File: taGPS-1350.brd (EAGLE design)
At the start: 49.9 x 61.5 mm, 86 parts, among them IC1 MSP430FR698X(1)80-PIN_PN, IC3 FT232RL

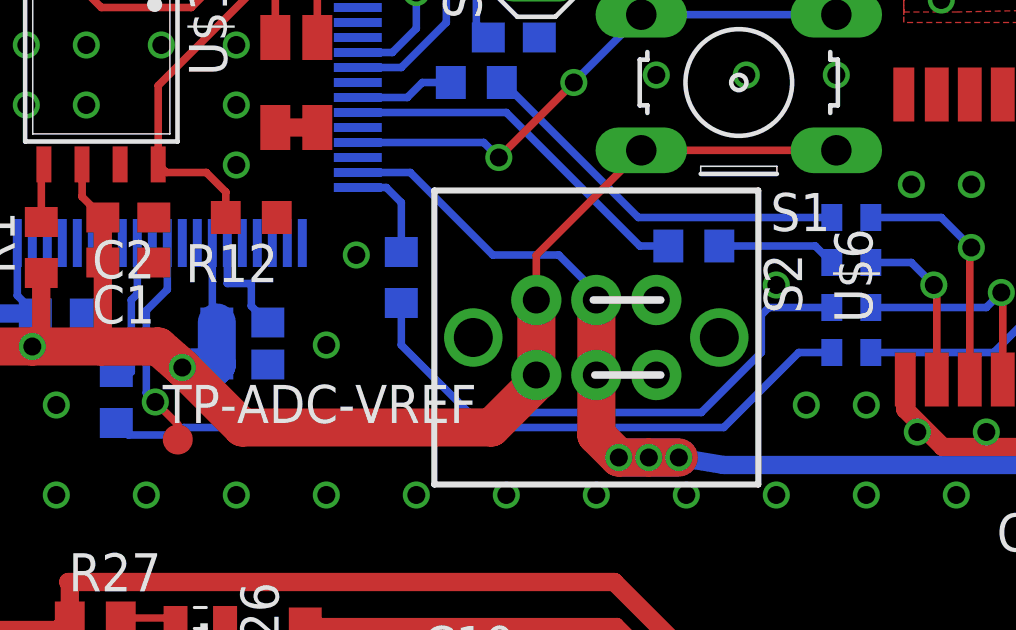
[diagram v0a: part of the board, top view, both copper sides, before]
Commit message: Fix 1350.brd timepulse resistor position
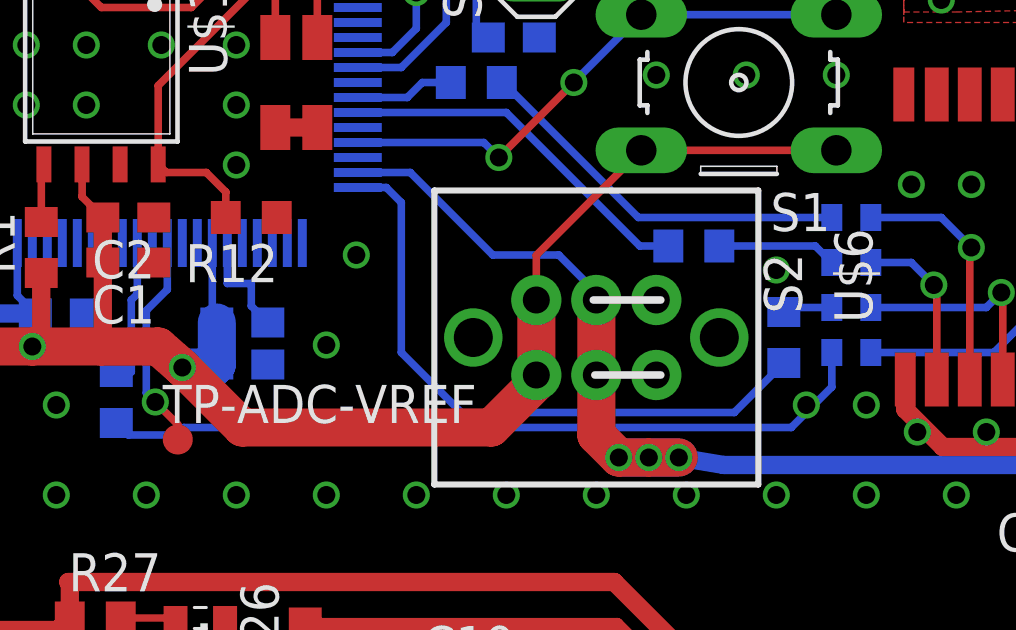
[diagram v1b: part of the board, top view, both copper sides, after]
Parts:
- moved R35 12.9 mm to (33.2, 33.2), turned to 90 degrees
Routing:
- net MB-GPS-TIMEPULSE: track 3.31 -> 20.9 mm
- net N$47: track 18.9 -> 1.75 mm
- net N$46: track 25.2 -> 25.8 mm
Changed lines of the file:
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@@
 <attribute name="SPICEPREFIX" value="C" x="64.25" y="39.35" size="1.778" layer="27" rot="R180" display="off"/>
 </element>
-<element name="R35" library="tagps" package="R0603" value="0" x="20.5" y="35.25" rot="MR270">
-<attribute name="SPICEPREFIX" value="R" x="40.6" y="51.95" size="1.778" layer="28" rot="MR270" display="off"/>
+<element name="R35" library="tagps" package="R0603" value="0" x="33.25" y="33.25" rot="MR90">
+<attribute name="SPICEPREFIX" value="R" x="13.15" y="16.55" size="1.778" layer="28" rot="MR90" display="off"/>
 </element>
 <element name="JP1" library="tagps" package="1X04" value="" x="23.9" y="1.7"/>
@@
 <via x="36" y="31" extent="1-16" drill="0.6"/>
 <via x="34" y="31" extent="1-16" drill="0.6"/>
-<via x="33" y="35" extent="1-16" drill="0.6"/>
+<via x="33" y="35.5" extent="1-16" drill="0.6"/>
 <via x="35" y="42" extent="1-16" drill="0.6"/>
 <via x="32" y="42" extent="1-16" drill="0.6"/>
@@
 <wire x1="20" y1="38.25" x2="19.05" y2="38.25" width="0.254" layer="16"/>
 <wire x1="20" y1="38.25" x2="20.5" y2="37.75" width="0.254" layer="16"/>
-<wire x1="20.5" y1="37.75" x2="20.5" y2="36.1" width="0.254" layer="16"/>
+<wire x1="33.25" y1="32.4" x2="31.6" y2="30.75" width="0.254" layer="16"/>
+<wire x1="31.6" y1="30.75" x2="22.5" y2="30.75" width="0.254" layer="16"/>
+<wire x1="22.5" y1="30.75" x2="20.5" y2="32.75" width="0.254" layer="16"/>
+<wire x1="20.5" y1="32.75" x2="20.5" y2="37.75" width="0.254" layer="16"/>
 </signal>
 <signal name="MB-GPS-TX">
@@
 <wire x1="11.4" y1="30" x2="13" y2="30" width="0.254" layer="16"/>
 <wire x1="13" y1="30" x2="13.25" y2="30.25" width="0.254" layer="16"/>
-<wire x1="13.25" y1="30.25" x2="31.25" y2="30.25" width="0.254" layer="16"/>
-<wire x1="31.25" y1="30.25" x2="33.75" y2="32.75" width="0.254" layer="16"/>
-<wire x1="33.75" y1="32.75" x2="34.85" y2="32.75" width="0.254" layer="16"/>
+<wire x1="13.25" y1="30.25" x2="33.5" y2="30.25" width="0.254" layer="16"/>
+<wire x1="34.85" y1="32.75" x2="34.85" y2="31.6" width="0.254" layer="16"/>
+<wire x1="34.85" y1="31.6" x2="33.5" y2="30.25" width="0.254" layer="16"/>
 </signal>
 <signal name="N$47">
 <contactref element="R35" pad="2"/>
-<wire x1="20.5" y1="33" x2="20.5" y2="34.4" width="0.254" layer="16"/>
-<wire x1="30.5" y1="30.75" x2="22.75" y2="30.75" width="0.254" layer="16"/>
-<wire x1="22.75" y1="30.75" x2="20.5" y2="33" width="0.254" layer="16"/>
-<wire x1="32.75" y1="34.25" x2="32.5" y2="34" width="0.254" layer="16"/>
-<wire x1="32.5" y1="34" x2="32.5" y2="32.75" width="0.254" layer="16"/>
-<wire x1="32.5" y1="32.75" x2="30.5" y2="30.75" width="0.254" layer="16"/>
 <contactref element="FB2" pad="2"/>
-<wire x1="34.85" y1="34.25" x2="32.75" y2="34.25" width="0.254" layer="16"/>
+<wire x1="34.85" y1="34.25" x2="33.25" y2="34.25" width="0.254" layer="16"/>
+<wire x1="33.25" y1="34.25" x2="33.25" y2="34.1" width="0.254" layer="16"/>
 </signal>
 <signal name="MB-PWR_GPS_SENSE">

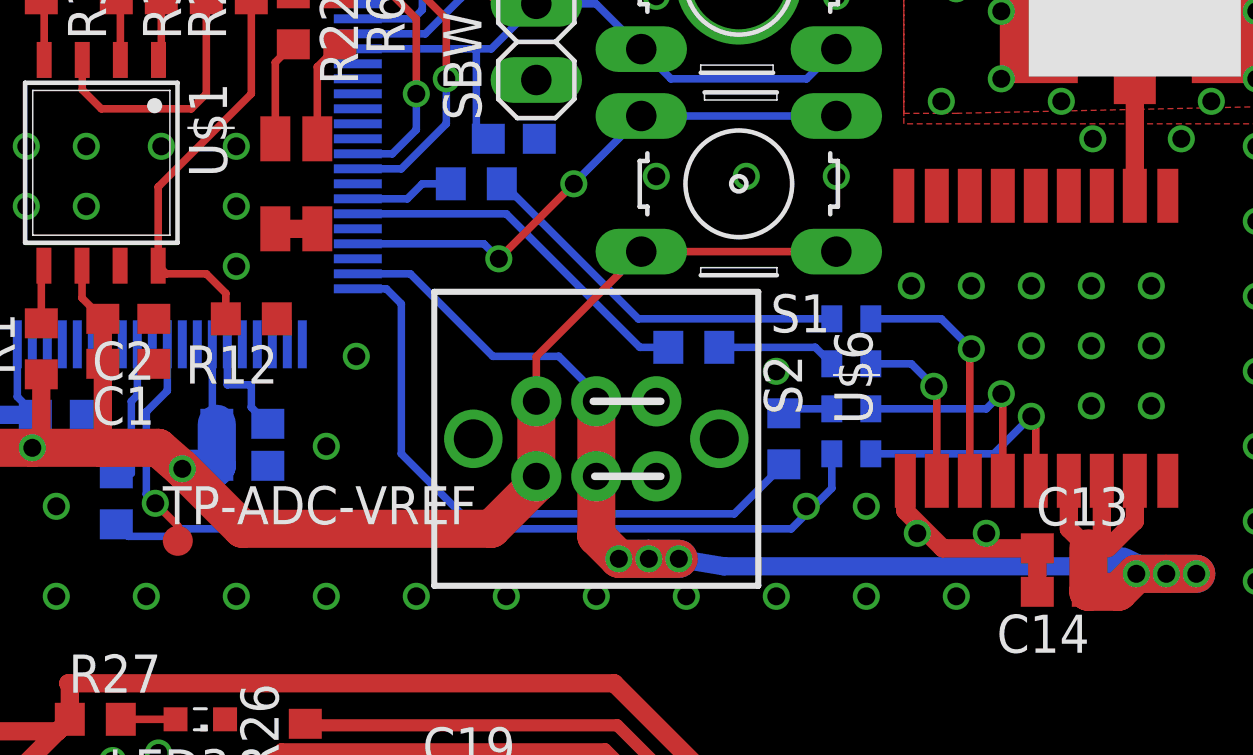
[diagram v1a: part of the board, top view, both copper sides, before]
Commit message: Improve 1350.brd gps chip inductors position
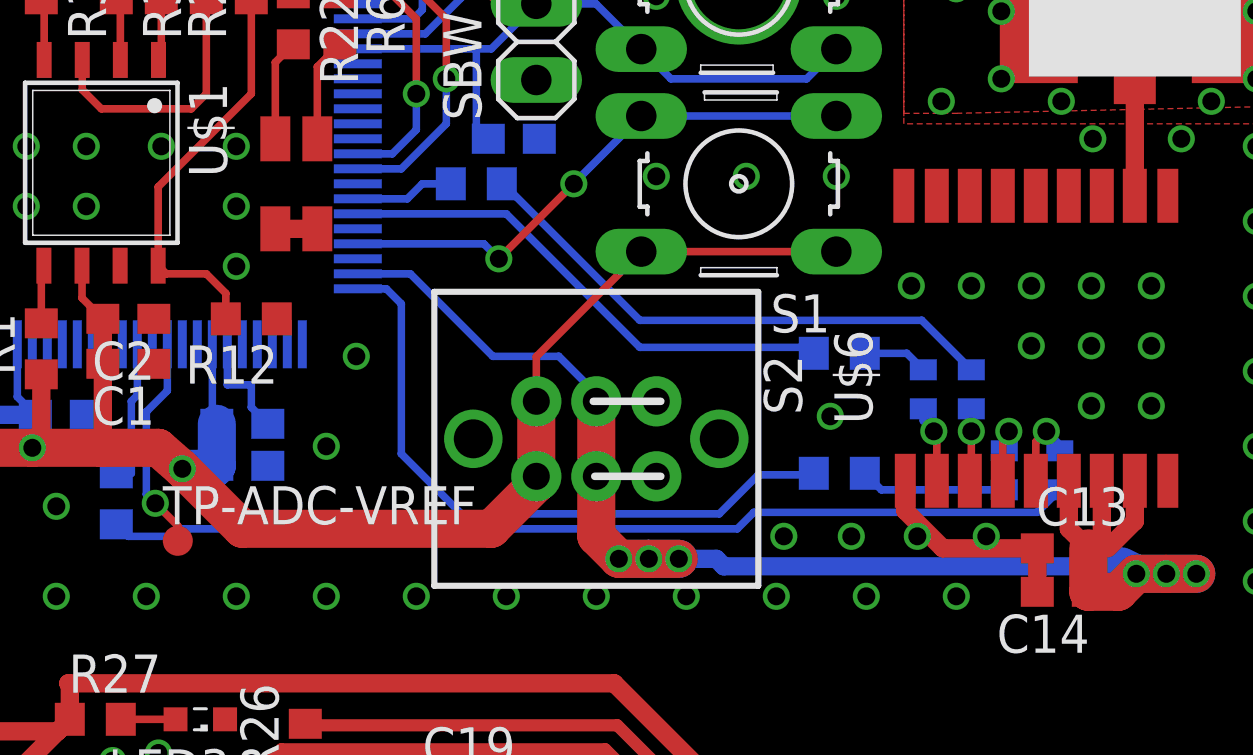
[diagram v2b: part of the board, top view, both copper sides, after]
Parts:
- moved FB3 6.97 mm to (42.5, 32.2), turned to 270 degrees
- moved FB2 5.50 mm to (40.6, 32.2), turned to 270 degrees
- moved R28 4.85 mm to (35.1, 36.1)
- moved FB0 4.64 mm to (39.5, 34.9), turned to 270 degrees
- moved FB1 2.55 mm to (37.9, 34.9), turned to 270 degrees
- moved R35 2.18 mm to (35.1, 32.1), turned to 180 degrees
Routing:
- net N$46: track 25.8 -> 32.3 mm
- net N$15: track 8.18 -> 2.42 mm
- net MB-GPS-RX: track 12.9 -> 18.2 mm
- net N$50: track 8.08 -> 2.84 mm
- net N$49: track 7.48 -> 2.52 mm
- net N$45: track 12.2 -> 17.1 mm
- net N$47: track 1.75 -> 4.88 mm
- net N$26: track 5.60 -> 2.59 mm
- net MB-GPS-TX: track 3.98 -> 2.18 mm
- net MB-GPS-TIMEPULSE: track 20.9 -> 21.8 mm
